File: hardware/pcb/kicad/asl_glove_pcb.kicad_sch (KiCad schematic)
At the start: 0 parts

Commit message: Update schematic
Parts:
- added J1: THUMB_FLEX, symbol Connector_Generic:Conn_01x02
- added J2: INDEX_FLEX, symbol Connector_Generic:Conn_01x02
- added J3: MIDDLE_FLEX, symbol Connector_Generic:Conn_01x02
- added J4: RING_FLEX, symbol Connector_Generic:Conn_01x02
- added J5: PINKY_FLEX, symbol Connector_Generic:Conn_01x02
- added J6: MPU6050_MODULE, symbol Connector_Generic:Conn_01x04
- added J7: ESP32_S3_DEVKIT_LEFT, symbol Connector_Generic:Conn_01x20
- added J8: ESP32_S3_DEVKIT_RIGHT, symbol Connector_Generic:Conn_01x20
- added R1, R2, R3, R4, R5: 10K, symbol Device:R
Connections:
- new net +3.3V: J1.2 (Pin_2), J2.2 (Pin_2), J3.2 (Pin_2), J4.2 (Pin_2), J5.2 (Pin_2), J6.1 (Pin_1), J8.1 (Pin_1)
- new net GND: J6.2 (Pin_2), J7.1 (Pin_1), R1.2, R2.2, R3.2, R4.2, R5.2
- new net I2C_SCL: J6.4 (Pin_4)
- new net I2C_SDA: J6.3 (Pin_3)
- new net INDEX_ADC: J2.1 (Pin_1), J7.18 (Pin_18), R2.1
- new net MIDDLE_ADC: J3.1 (Pin_1), J8.3 (Pin_3), R3.1
- new net PINKY_ADC: J5.1 (Pin_1), J8.5 (Pin_5), R5.1
- new net RING_ADC: J4.1 (Pin_1), J8.4 (Pin_4), R4.1
- new net THUMB_ADC: J1.1 (Pin_1), J7.19 (Pin_19), R1.1
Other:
- company: (none) -> Maxim Kisselev
- title: (none) -> ASL Glove PCB

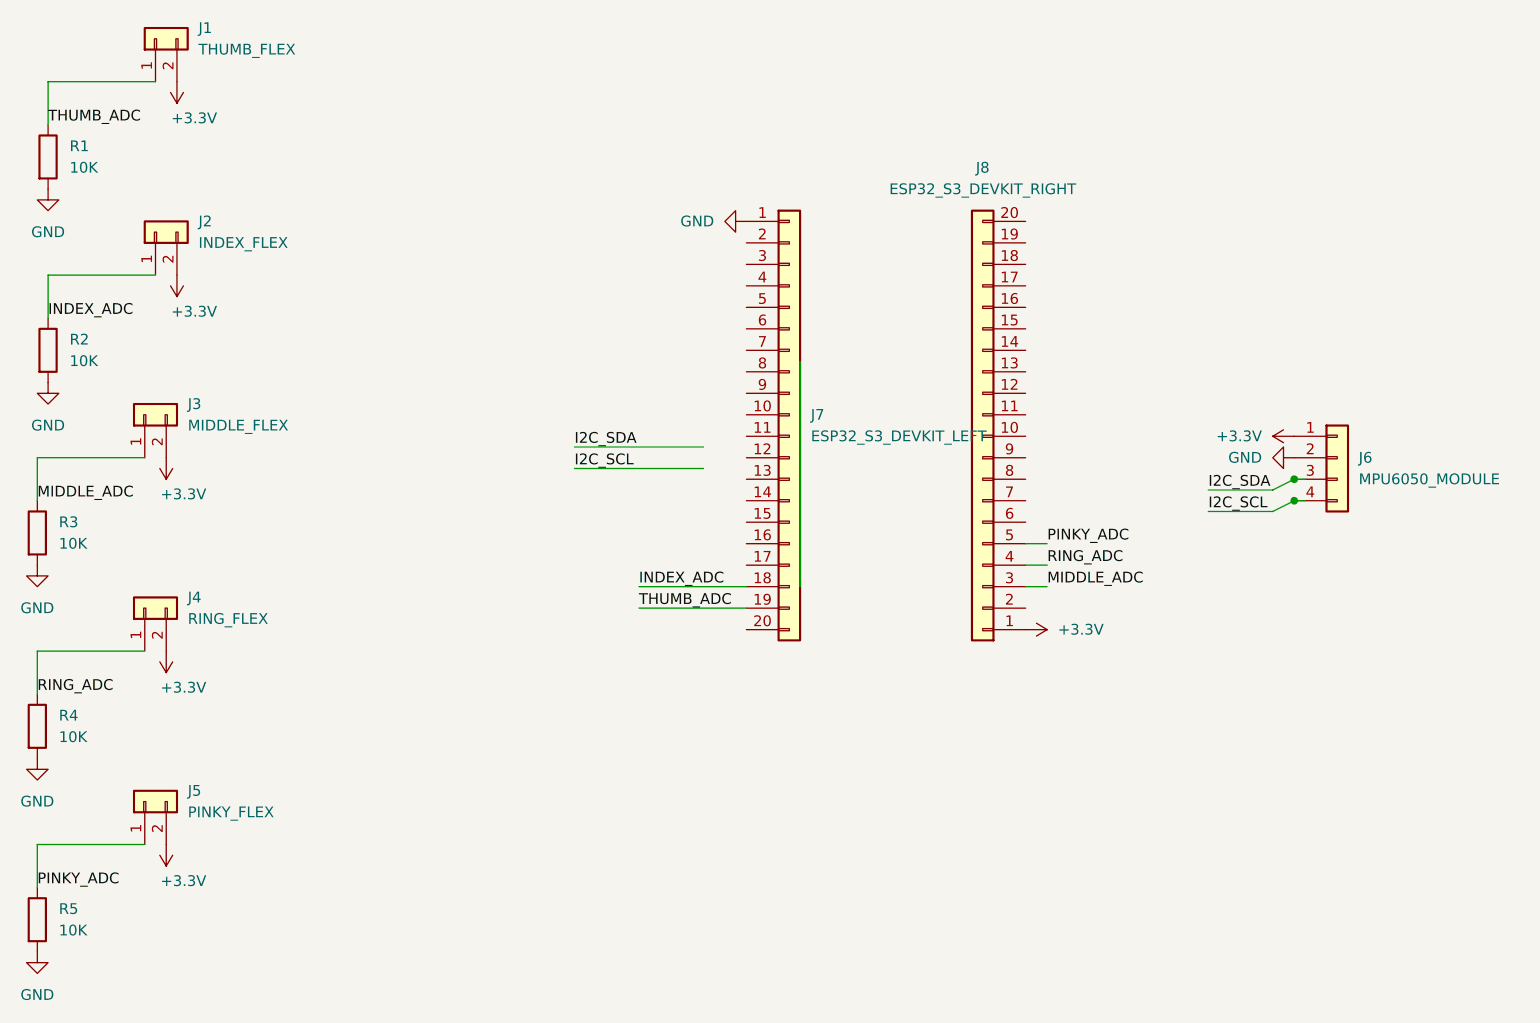
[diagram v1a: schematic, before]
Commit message: Finished schematic and PCB for only flex sensors, but without touch sensors between fingers
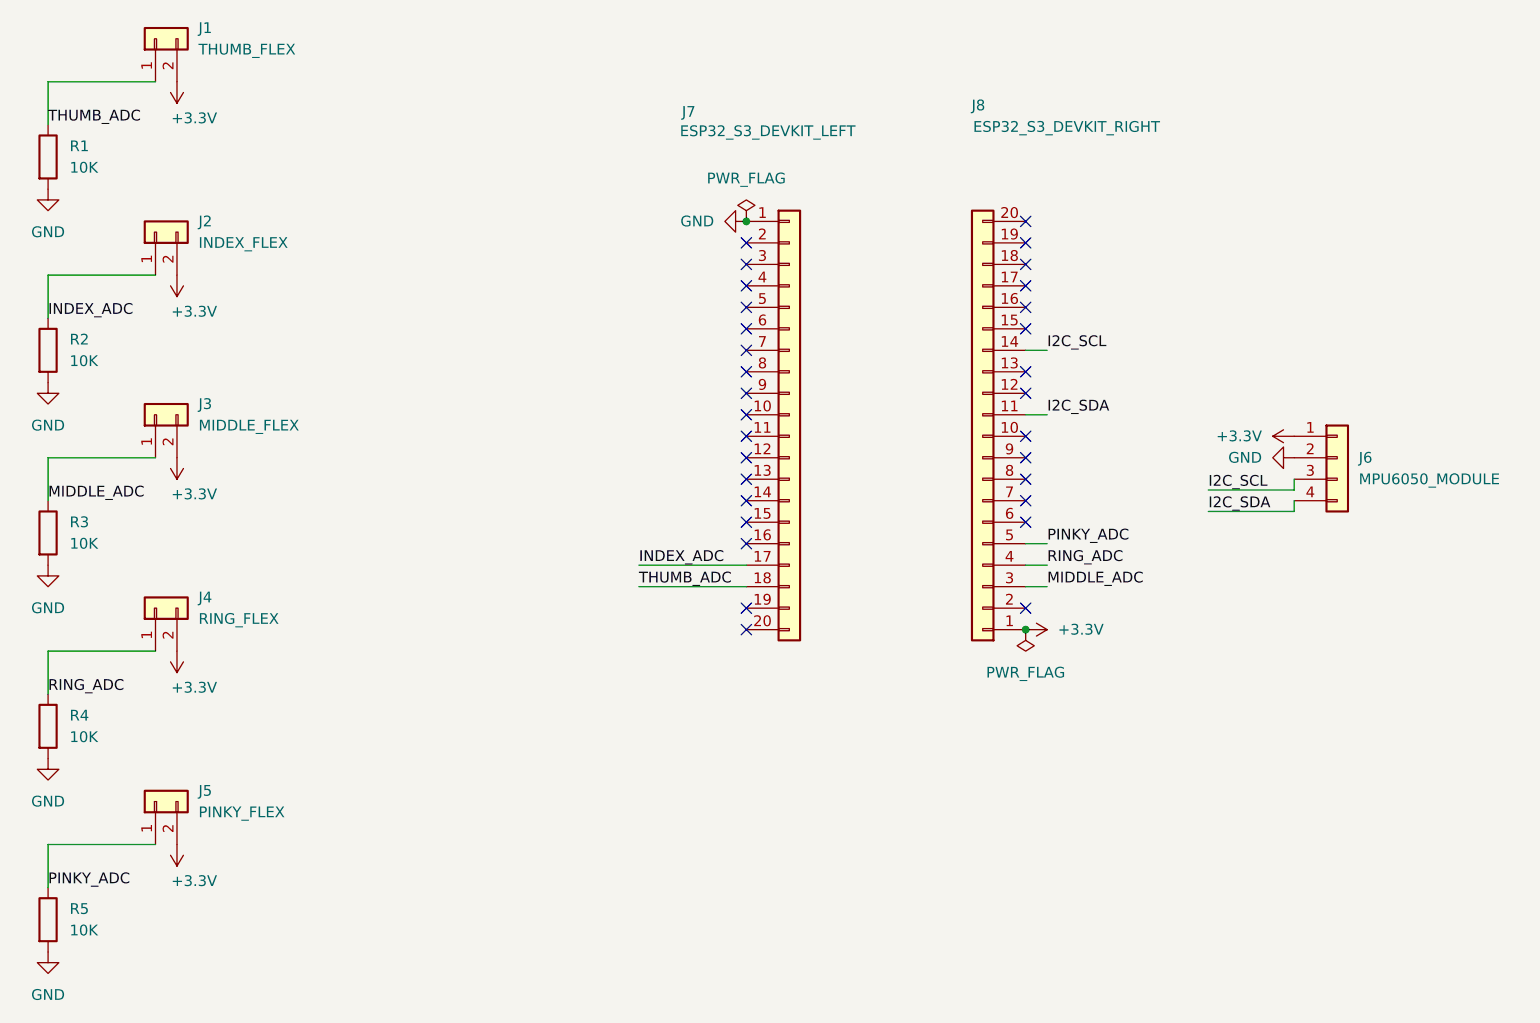
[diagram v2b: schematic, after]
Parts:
- J1, J2, J3, J4, J5: footprint (none) -> Connector_PinHeader_2.54mm:PinHeader_1x02_P2.54mm_Vertical
- J6: footprint (none) -> Connector_PinHeader_2.54mm:PinHeader_1x04_P2.54mm_Vertical
- J7, J8: footprint (none) -> Connector_PinHeader_2.54mm:PinHeader_1x20_P2.54mm_Vertical
- R1, R2, R3, R4, R5: footprint (none) -> Resistor_THT:R_Axial_DIN0207_L6.3mm_D2.5mm_P7.62mm_Horizontal
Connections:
- net I2C_SCL: now also J6.3 (Pin_3), J8.14 (Pin_14); no longer J6.4 (Pin_4)
- net I2C_SDA: now also J6.4 (Pin_4), J8.11 (Pin_11); no longer J6.3 (Pin_3)
- net INDEX_ADC: now also J7.17 (Pin_17); no longer J7.18 (Pin_18)
- net THUMB_ADC: now also J7.18 (Pin_18); no longer J7.19 (Pin_19)
- no-connect marks 0 -> 31
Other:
- moved on the sheet: J3, J4, J5, R3, R4, R5
